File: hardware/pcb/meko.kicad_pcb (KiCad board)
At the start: 6 copper layers, 50.2 x 77.2 mm, 287 parts, among them IC1 MCP16502AB, IC2 MAYA-W386-00B, IC3 TAC5212, J1 Conn_01x02_Pin, J2 Conn_ARM_JTAG_SWD_10, J3 USB_C_Receptacle_USB2.0_16P, J4 PJ-342, J5 PJ-242, J6 Micro_SD_Card_Det2, J7 Micro_SD_Card_Det1, J8 503480-1000, J9 503480-0540, SW1 SW_Push_Shielded, SW2 SW_Push_Shielded, SW3 SW_Push_Shielded, SW4 SW_Push_Shielded, SW5 SW_Push_Shielded, U1 SAMA7D65-4HB, U2 MT41K256M16TW, U3 TPS7A2033PDBV, U4 BQ25640, U5 MAX17260, U6 ECMF02-2AMX6, U7 DRV2605LDGS, Y1 24MHz, Y2 32kHz768, Y3 32kHz768

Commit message: laid out caps for vdd ddr, added custom rule area for bgas
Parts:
- added C128: 100n, Capacitor_SMD:C_0201_0603Metric, F.Cu at (191.9, 162.8)
- added R57: 10k, Resistor_SMD:R_0402_1005Metric, F.Cu at (149.2, 144.2)
- R17: footprint Resistor_SMD:R_0402_1005Metric -> Resistor_SMD:R_0201_0603Metric
- moved C64 216.9 mm to (242.8, 136.6)
- moved C66 216.9 mm to (242.8, 138.3)
- moved R15 216.4 mm to (244.9, 136.6)
- moved R16 216.4 mm to (244.9, 138.6)
- moved C65 214.3 mm to (244.8, 140.5)
- moved C11 202.7 mm to (203.1, 169.4)
- moved C19 200.8 mm to (196.2, 161.1)
- moved C15 199.2 mm to (191.9, 156.8), turned to 90 degrees
- moved C27 198.1 mm to (193.8, 159.1), turned to 180 degrees
- moved C37 198.0 mm to (196.2, 159.1), turned to 180 degrees
- moved R18 195.7 mm to (224.4, 139.6)
- moved C40 195.1 mm to (194.2, 162.1)
- moved C23 194.2 mm to (193.9, 160.4), turned to -90 degrees
- moved C46 194.0 mm to (193.8, 156.8), turned to 90 degrees
- moved C67 194.0 mm to (224.4, 140.7)
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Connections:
- net Net-(U1DDR-DDR_ZQ) renamed /SAMA7/ZQ
- net Net-(U2-ZQ) renamed /DDR/ZQ
- J9 pad 1: /SAMA7/TOUCH_~{INT} -> +3V3
- J9 pad 2: +3V3 -> /SAMA7/TOUCH_~{INT}
- U1 pad C18: unconnected-(U1GPIO C&D&E-PD14-PadC18) -> /SAMA7/BT.HOST_WAKE
- U1 pad E18: unconnected-(U1GPIO C&D&E-PD16-PadE18) -> /SAMA7/BT.EN
- U1 pad H12: unconnected-(U1GPIO C&D&E-PD15-PadH12) -> /SAMA7/BT.DEV_WAKE
- U1 pad L14: /SAMA7/BT.HOST_WAKE -> unconnected-(U1GPIO A&B-PB19-PadL14)
- U1 pad M12: /SAMA7/BT.DEV_WAKE -> unconnected-(U1GPIO A&B-PB20-PadM12)
- U1 pad R19: /SAMA7/BT.EN -> unconnected-(U1GPIO A&B-PB11-PadR19)
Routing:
- net +1V35_DDR: track 0.00 -> 29.0 mm, vias 0 -> 32
- net GND: track 0.00 -> 28.4 mm, vias 0 -> 32
- net /DDR/CK+: track 0.00 -> 0.95 mm, vias 0 -> 1
- net /DDR/CK-: track 0.00 -> 0.94 mm, vias 0 -> 1
- net /DDR/~{CAS}: track 0.00 -> 0.64 mm, vias 0 -> 1
- net /DDR/~{RAS}: track 0.00 -> 0.45 mm, vias 0 -> 1

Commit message: ddr routing, and mucking around
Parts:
- C14, C23, C27, C34, C42, C50, C52: footprint Capacitor_SMD:C_0201_0603Metric -> PCM_ckl-misc:C_0201_0603Metric_Dense
- C64, C66: moved to B.Cu
- R15, R16: footprint Resistor_SMD:R_0402_1005Metric -> Resistor_SMD:R_0201_0603Metric; moved to B.Cu
- R18: footprint Resistor_SMD:R_0402_1005Metric -> Resistor_SMD:R_0201_0603Metric
- moved C14 189.8 mm to (189.9, 156.8), turned to 90 degrees
- moved R3 185.1 mm to (198.0, 156.5)
- moved R15 47.9 mm to (200.6, 154.7), turned to 135 degrees
- moved C64 46.6 mm to (200.1, 155.2), turned to -45 degrees
- moved R16 46.5 mm to (201.1, 154.2), turned to -45 degrees
- moved C66 44.0 mm to (201.6, 153.7), turned to 135 degrees
- moved R18 32.0 mm to (194.3, 150.1), turned to 90 degrees
- moved C65 4.46 mm to (249.0, 138.9)
- moved C50 1.94 mm to (193.5, 159.4)
- moved C42 1.04 mm to (191.7, 160.8)
- moved C84 0.62 mm to (202.6, 144.6)
- moved C27 0.43 mm to (193.5, 158.8)
- moved C34 0.34 mm to (191.2, 158.9)
- moved C52 0.33 mm to (192.6, 160.1)
- moved C37 0.30 mm to (196.5, 159.1)
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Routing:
- net /DDR/DQ7: track 0.00 -> 38.8 mm
- net /DDR/DQM0: track 0.00 -> 38.4 mm
- net /DDR/DQ5: track 0.00 -> 38.3 mm
- net /DDR/DQ0: track 0.00 -> 38.3 mm
- net /DDR/DQ1: track 0.00 -> 37.7 mm
- net /DDR/DQ3: track 0.00 -> 37.7 mm
- net /DDR/DQ10: track 0.00 -> 34.5 mm
- net /DDR/DQ14: track 0.00 -> 32.5 mm
- net /DDR/DQ8: track 0.00 -> 30.7 mm
- net /DDR/DQ12: track 0.00 -> 28.5 mm
- net /DDR/DQS1+: track 0.00 -> 27.5 mm
- net /DDR/DQS1-: track 0.00 -> 27.1 mm
- net /DDR/DQM1: track 0.00 -> 27.0 mm
- net /DDR/DQ4: track 0.00 -> 26.4 mm
- net /DDR/DQ6: track 0.00 -> 24.8 mm
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
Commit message: removed ddr traces
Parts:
- moved C65 30.3 mm to (223.3, 155.0), turned to 45 degrees
- moved C66 22.5 mm to (224.0, 154.3)
- moved R15 22.5 mm to (223.0, 155.2)
- moved R16 22.5 mm to (223.5, 154.8)
- moved C64 22.5 mm to (222.5, 155.7)
- moved C11 21.5 mm to (224.6, 168.8)
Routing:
- net /DDR/DQ10: track 34.5 -> 1.47 mm
- net /DDR/DQ7: track 38.8 -> 6.46 mm
- net /DDR/DQ5: track 38.3 -> 7.03 mm
- net /DDR/DQ3: track 37.7 -> 7.46 mm
- net /DDR/DQ1: track 37.7 -> 7.61 mm
- net /DDR/DQ14: track 32.5 -> 2.71 mm
- net /DDR/DQ12: track 28.5 -> 0.80 mm
- net /DDR/DQM0: track 38.4 -> 11.3 mm
- net /DDR/DQ0: track 38.3 -> 12.6 mm
- net /DDR/DQ8: track 30.7 -> 5.81 mm
- net /DDR/DQS1-: track 27.1 -> 3.11 mm
- net /DDR/DQS1+: track 27.5 -> 4.05 mm
- net /DDR/DQM1: track 27.0 -> 6.03 mm
- net /DDR/DQ9: track 23.2 -> 4.10 mm
- net /DDR/DQ11: track 22.6 -> 4.87 mm
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
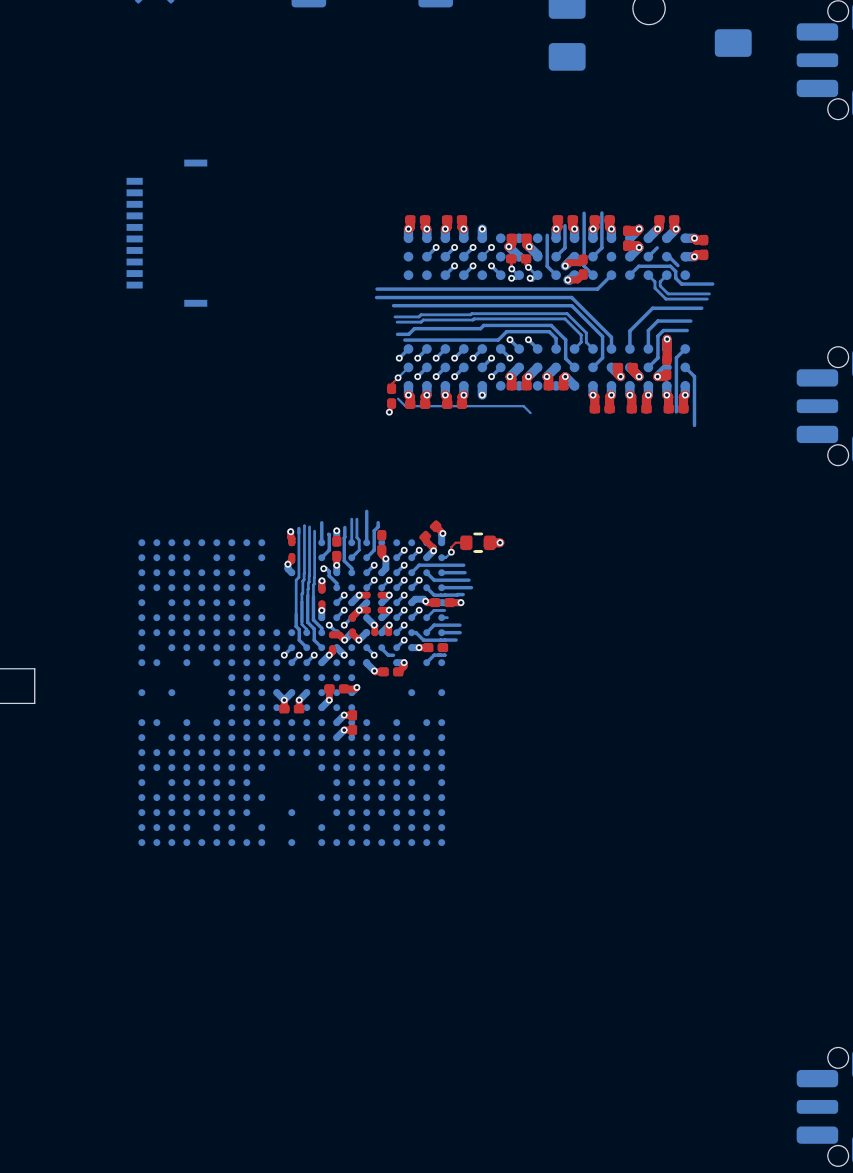
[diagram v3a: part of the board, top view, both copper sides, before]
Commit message: new layout for ram and mpu
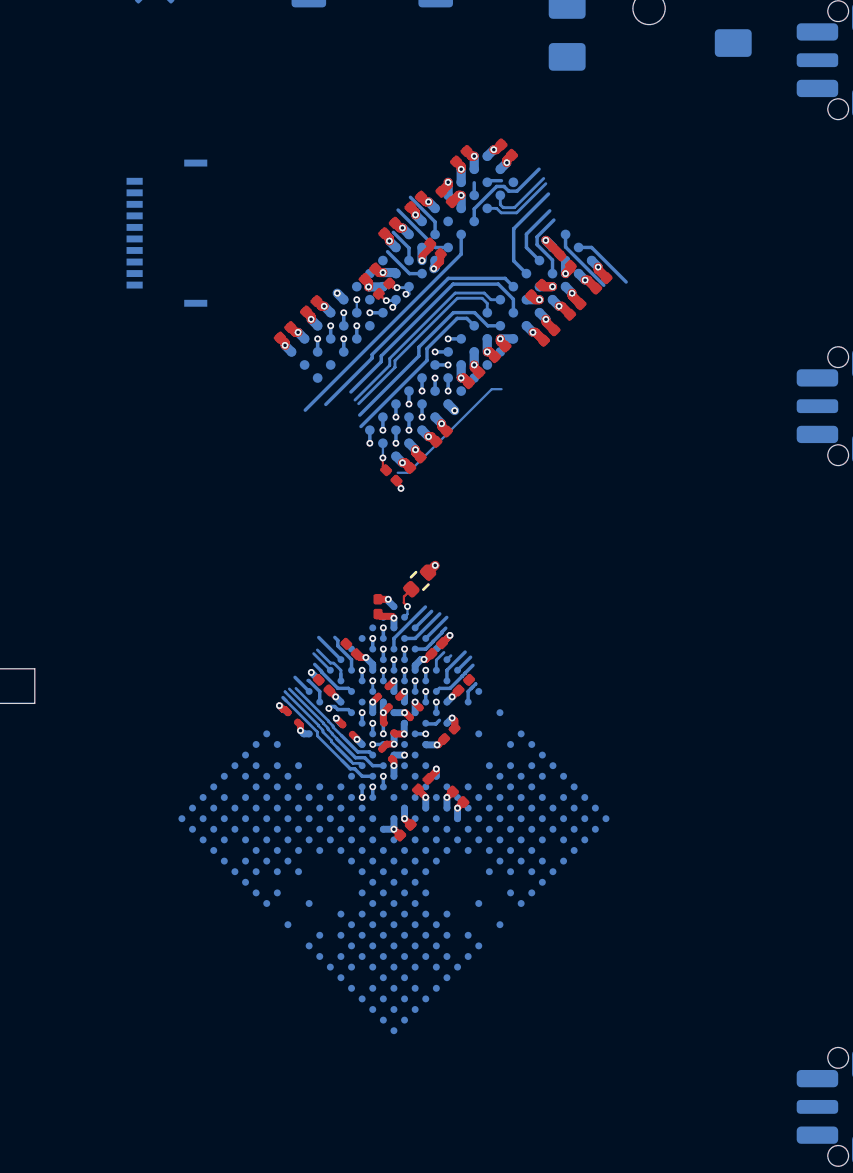
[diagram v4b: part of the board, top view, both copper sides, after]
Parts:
- moved C86 9.53 mm to (199.3, 139.5), turned to 135 degrees
- moved C81 9.33 mm to (197.3, 139.7), turned to 45 degrees
- moved C85 8.13 mm to (195.3, 141.7), turned to -135 degrees
- moved C79 8.05 mm to (196.6, 141.5), turned to -45 degrees
- moved C80 7.63 mm to (194.2, 142.9), turned to 45 degrees
- moved C87 7.54 mm to (189.6, 147.4), turned to -135 degrees
- moved C14 7.28 mm to (190.0, 164.1), turned to 135 degrees
- moved C82 7.26 mm to (190.8, 146.3), turned to -135 degrees
- moved C31 7.21 mm to (194.9, 169.0), turned to -135 degrees
- moved U1 7.03 mm to (194.4, 168.5), turned to -45 degrees
- moved C75 6.65 mm to (193.3, 144.8), turned to 45 degrees
- moved C84 6.45 mm to (196.2, 143.8), turned to 135 degrees
- moved C71 6.38 mm to (201.8, 144.3), turned to 135 degrees
- moved C69 6.33 mm to (203.4, 145.3), turned to -135 degrees
- moved R17 5.98 mm to (193.9, 145.5), turned to -135 degrees
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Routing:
- net /DDR/DQ2: track 13.2 -> 12.1 mm
- net /DDR/DQS0+: track 10.5 -> 9.55 mm
- net /DDR/DQS0-: track 11.2 -> 10.3 mm
- net /DDR/DQ0: track 12.6 -> 11.8 mm
- net /DDR/DQ6: track 10.4 -> 9.76 mm

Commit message: routed
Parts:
- moved J8 1.00 mm to (183.6, 143.1)
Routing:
- net /DDR/DQ1: track 7.61 -> 39.6 mm
- net /DDR/DQ3: track 7.46 -> 39.3 mm
- net /DDR/DQ5: track 7.03 -> 34.7 mm
- net /DDR/DQ7: track 6.46 -> 31.8 mm
- net /DDR/DQM0: track 11.3 -> 26.0 mm
- net /DDR/DQ0: track 11.8 -> 26.2 mm
- net /DDR/DQ2: track 12.1 -> 26.1 mm
- net /DDR/DQS0+: track 9.55 -> 21.7 mm
- net /DDR/DQS0-: track 10.3 -> 22.1 mm
- net /DDR/DQ6: track 9.76 -> 19.8 mm
- net /DDR/DQ4: track 9.01 -> 18.3 mm
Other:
- outline, holes or cut-outs redrawn

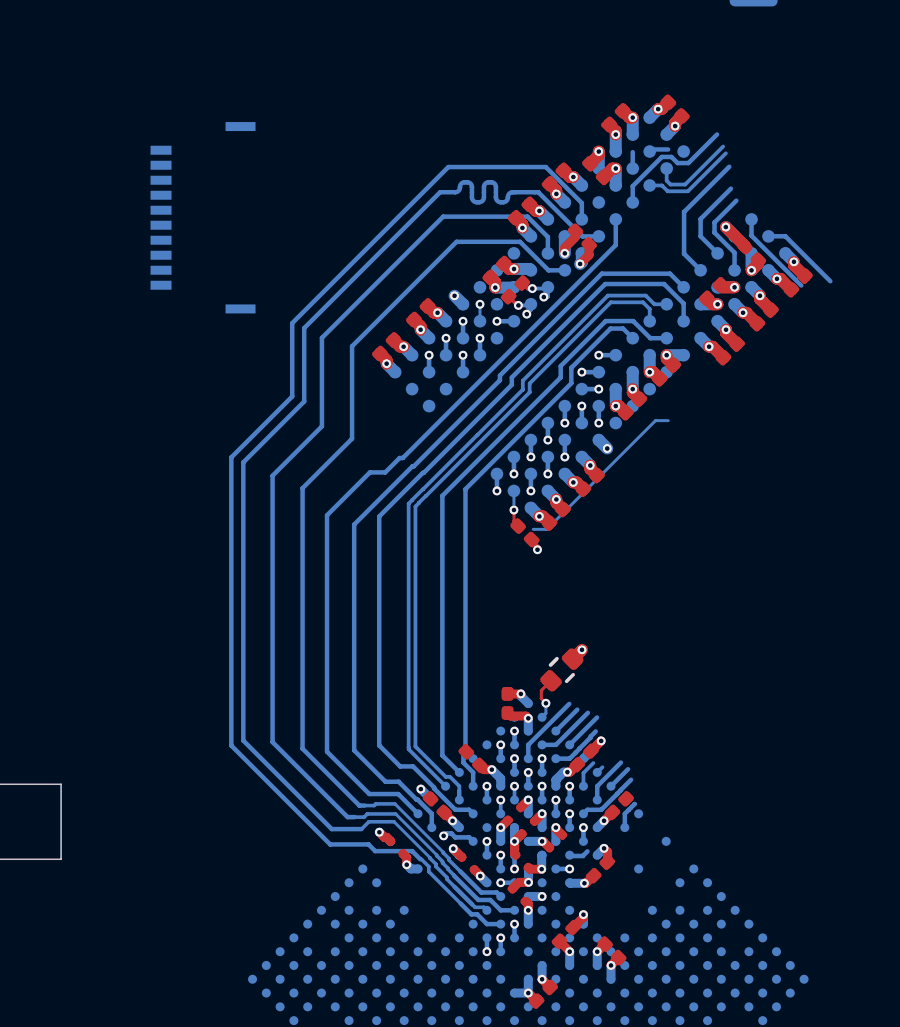
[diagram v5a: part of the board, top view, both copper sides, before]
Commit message: length matching
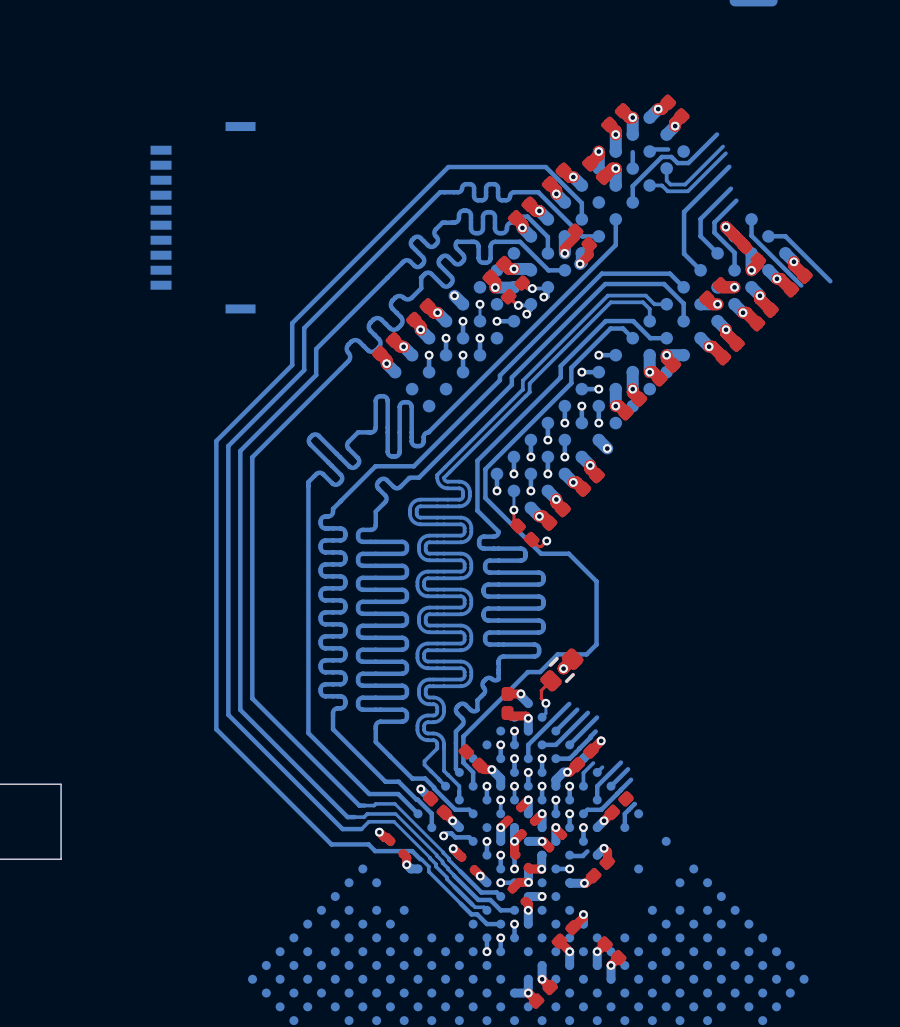
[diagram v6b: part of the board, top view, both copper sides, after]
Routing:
- net /DDR/DQ2: track 26.1 -> 50.8 mm
- net /DDR/DQ6: track 19.8 -> 38.1 mm
- net /DDR/DQS0+: track 21.7 -> 38.2 mm
- net /DDR/DQS0-: track 22.1 -> 38.1 mm
- net /DDR/DQM0: track 26.0 -> 38.2 mm
- net /DDR/DQ0: track 26.2 -> 38.1 mm
- net /DDR/DQ7: track 31.8 -> 39.3 mm
- net /DDR/~{RESET}: track 7.14 -> 1.14 mm
- net /DDR/DQ5: track 34.7 -> 39.4 mm
- net /DDR/DQ4: track 18.3 -> 22.7 mm

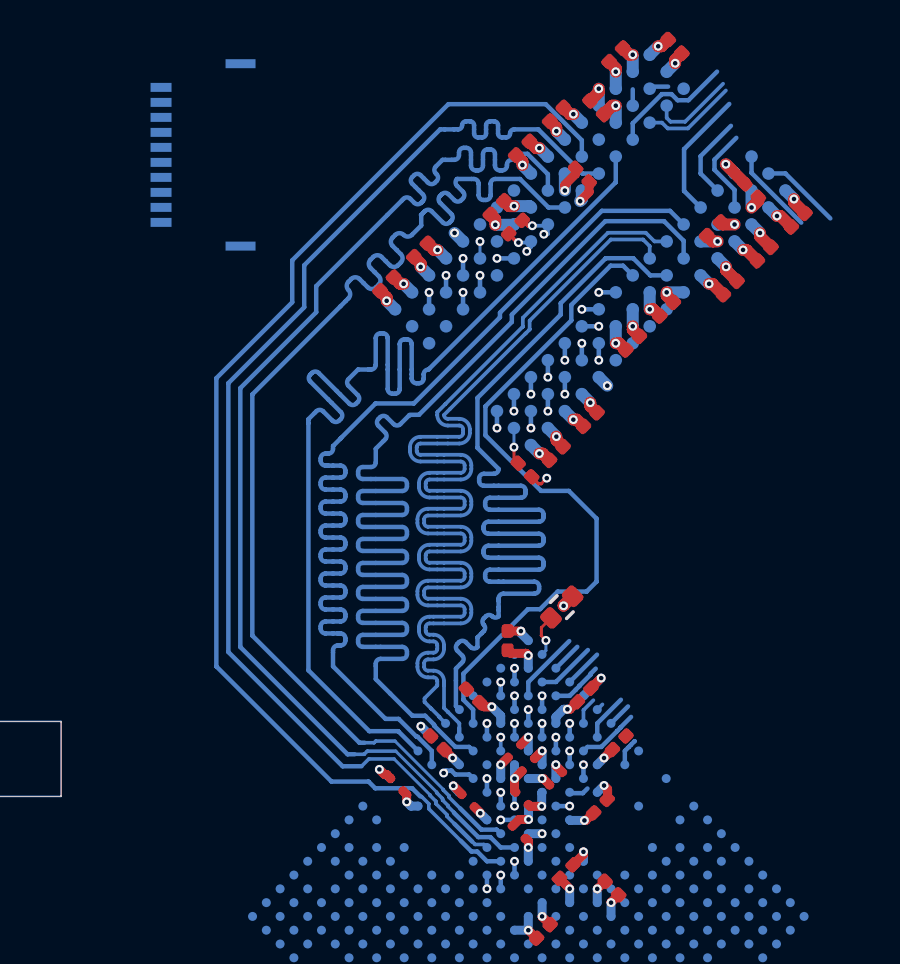
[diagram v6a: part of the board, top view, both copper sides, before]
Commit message: more length matching
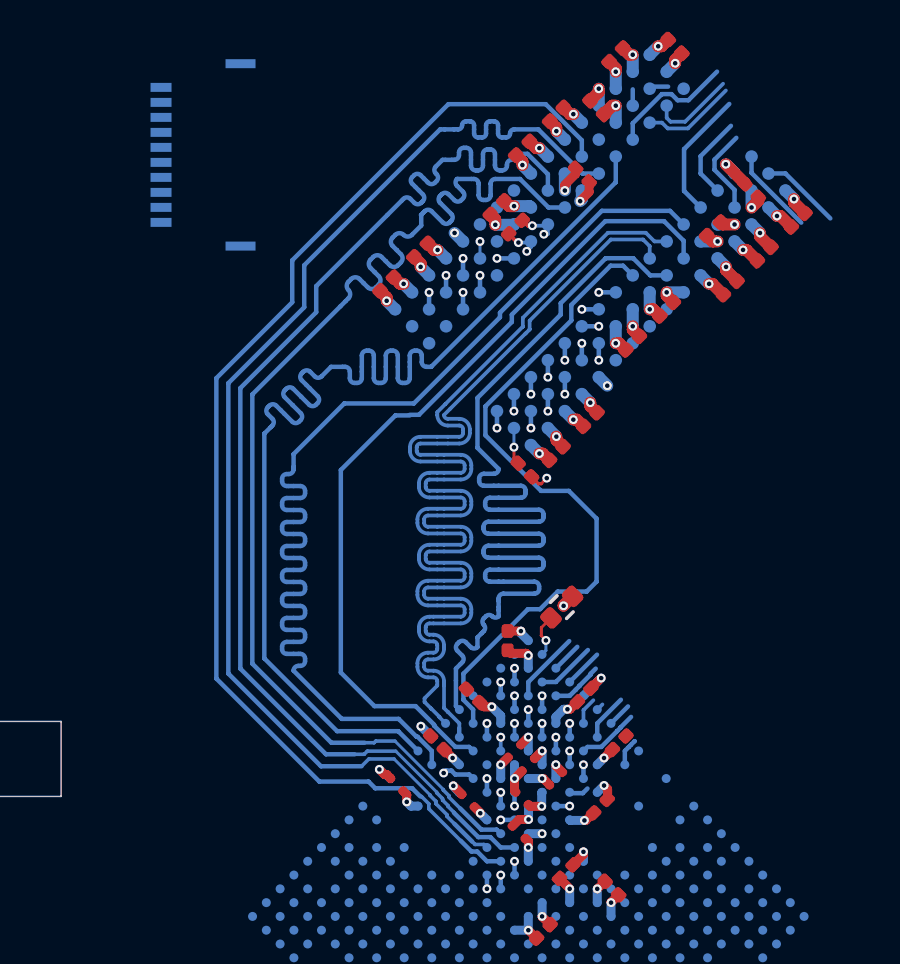
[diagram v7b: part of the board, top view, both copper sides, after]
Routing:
- net /DDR/DQ2: track 50.8 -> 28.1 mm
- net /DDR/DQ0: track 38.1 -> 39.8 mm
- net /DDR/DQM0: track 38.2 -> 39.8 mm
- net /DDR/DQ7: track 39.3 -> 39.9 mm

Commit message: ddr
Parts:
- turned J8 to 90 degrees
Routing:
- net /DDR/DQ4: track 22.7 -> 41.0 mm
- net /DDR/DQ2: track 28.1 -> 41.0 mm
- net /DDR/~{RESET}: track 1.14 -> 9.79 mm
- net /DDR/DQS0-: track 38.1 -> 41.6 mm
- net /DDR/DQ6: track 38.1 -> 40.9 mm
- net /DDR/DQS0+: track 38.2 -> 40.0 mm
- net /DDR/DQ5: track 39.8 -> 41.3 mm
- net /DDR/DQ7: track 39.9 -> 41.3 mm
- net /DDR/DQ0: track 39.8 -> 41.1 mm
- net /DDR/DQ1: track 39.8 -> 41.1 mm
- net /DDR/DQM0: track 39.8 -> 41.1 mm
- net /DDR/DQ3: track 39.9 -> 41.2 mm
